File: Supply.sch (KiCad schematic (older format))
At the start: 7 parts, among them P5 CONN_01X02, Q5 AO3401, U3 EPL3015, U4 TPS61222

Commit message: Fix Boot0 pin and add prices per component
Signed-off-by: Philip Luyckx <philip.luyckx@gmail.com>
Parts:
- C8, C9: Price (none) -> 0.02
- Q5: Price (none) -> 0.06
- R11: Price (none) -> 0.01
- U3: Price (none) -> 1.15
- U4: Price (none) -> 1.00
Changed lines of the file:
@@
 F 2 "CustomSmd:SOT23" H 2900 2290 60  0001 C CNN
 F 3 "" H 2900 2290 60  0000 C CNN
+F 4 "0.06" H 3350 2150 60  0001 C CNN "Price"
 	1    3350 2150
 	0    1    -1   0
@@
 F 2 "Resistors_SMD:R_0603" V 2930 2450 30  0001 C CNN
 F 3 "" H 3000 2450 30  0000 C CNN
+F 4 "0.01" V 3000 2450 60  0001 C CNN "Price"
 	1    3000 2450
 	0    1    1    0
@@
 F 2 "Resistors_SMD:R_0805" H 3888 2150 30  0001 C CNN
 F 3 "" H 3850 2300 60  0000 C CNN
+F 4 "0.02" H 3850 2300 60  0001 C CNN "Price"
 	1    3850 2300
 	1    0    0    -1
@@
 F 2 "CustomInductors:EPL3015" H 4200 2050 60  0001 C CNN
 F 3 "" H 4200 2050 60  0000 C CNN
+F 4 "1.15" V 4200 2050 60  0001 C CNN "Price"
 	1    4200 2050
 	0    -1   -1   0
@@
 F 2 "Resistors_SMD:R_0805" H 5788 2050 30  0001 C CNN
 F 3 "" H 5750 2200 60  0000 C CNN
+F 4 "0.02" H 5750 2200 60  0001 C CNN "Price"
 	1    5750 2200
 	1    0    0    -1
@@
 F 2 "DC_DC_Converters:TPS6122x" H 4950 1900 60  0001 C CNN
 F 3 "" H 4950 1900 60  0000 C CNN
+F 4 "1.00" H 4950 1900 60  0001 C CNN "Price"
 	1    4950 1900
 	1    0    0    -1

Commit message: Update schematics for V3:
 * Change DHT22 to HTU21D
 * Change schematic for MCP6044
 * Correct unused opamp + power supply
 * Reassign some cpu pins (for HTU21D)
 * Add LDO power supply for 1.8V
 * Update STM32CubeMx project
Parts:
- added C17: 0.1uF, symbol C
- added C18: 0.47uF, symbol C
- added R15: 100k, symbol R
- added U4: TPS79718, symbol TPS79718
- renumbered C8 to C19, C9 to C20, P5 to P3, Q5 to Q2, R11 to R14, U3 to U5, U4 to U6
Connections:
- net +BATT: now also C17.1, U4.4 (IN)
- net GND: now also C17.2, C18.2, U4.2 (GND)
- new net: R15.1, U4.1 (PG)
- new net +1V8: C18.1, R15.2, U4.5 (OUT)
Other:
- note added: "1V8 Supply\n"
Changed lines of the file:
@@
 LIBS:CustomModules
 LIBS:CustomPower
-LIBS:CustomPowerConvertors
 LIBS:CustomTransistors
 LIBS:Custom_ShiftRegisters
@@
 LIBS:Relais
 LIBS:CustomDevices
+LIBS:CustomPowerConvertors
 LIBS:Sensor-cache
 EELAYER 25 0
@@
 $EndDescr
 $Comp
-L CONN_01X02 P5
+L CONN_01X02 P3
 U 1 1 56630FD4
 P 1800 2100
-F 0 "P5" H 1800 2250 50  0000 C CNN
+F 0 "P3" H 1800 2250 50  0000 C CNN
 F 1 "CONN_01X02" V 1900 2100 50  0000 C CNN
 F 2 "Socket_Strips:Socket_Strip_Straight_1x02" H 1800 2100 60  0001 C CNN
@@
 $EndComp
 $Comp
-L +BATT #PWR034
+L +BATT #PWR35
 U 1 1 56631049
 P 1600 2050
-F 0 "#PWR034" H 1600 1900 50  0001 C CNN
+F 0 "#PWR35" H 1600 1900 50  0001 C CNN
 F 1 "+BATT" H 1600 2190 50  0000 C CNN
 F 2 "" H 1600 2050 60  0000 C CNN
@@
 $EndComp
 $Comp
-L GND #PWR035
+L GND #PWR36
 U 1 1 5663105F
 P 1600 2150
-F 0 "#PWR035" H 1600 1900 50  0001 C CNN
+F 0 "#PWR36" H 1600 1900 50  0001 C CNN
 F 1 "GND" H 1600 2000 50  0000 C CNN
 F 2 "" H 1600 2150 60  0000 C CNN
@@
 	1400 2400 1400 1800
 $Comp
-L +BATT #PWR036
+L +BATT #PWR34
 U 1 1 56635CFE
 P 1500 1000
-F 0 "#PWR036" H 1500 850 50  0001 C CNN
+F 0 "#PWR34" H 1500 850 50  0001 C CNN
 F 1 "+BATT" H 1500 1140 50  0000 C CNN
 F 2 "" H 1500 1000 60  0000 C CNN
@@
 $EndComp
 $Comp
-L GND #PWR037
+L GND #PWR33
 U 1 1 56635D42
 P 1100 1050
-F 0 "#PWR037" H 1100 800 50  0001 C CNN
+F 0 "#PWR33" H 1100 800 50  0001 C CNN
 F 1 "GND" H 1100 900 50  0000 C CNN
 F 2 "" H 1100 1050 60  0000 C CNN
@@
 $EndComp
 $Comp
-L PWR_FLAG #FLG038
+L PWR_FLAG #FLG1
 U 1 1 56635D80
 P 1100 1050
-F 0 "#FLG038" H 1100 1145 50  0001 C CNN
+F 0 "#FLG1" H 1100 1145 50  0001 C CNN
 F 1 "PWR_FLAG" H 1100 1230 50  0000 C CNN
 F 2 "" H 1100 1050 60  0000 C CNN
@@
 $EndComp
 $Comp
-L PWR_FLAG #FLG039
+L PWR_FLAG #FLG2
 U 1 1 56635DC4
 P 1650 1000
-F 0 "#FLG039" H 1650 1095 50  0001 C CNN
+F 0 "#FLG2" H 1650 1095 50  0001 C CNN
 F 1 "PWR_FLAG" H 1650 1180 50  0000 C CNN
 F 2 "" H 1650 1000 60  0000 C CNN
@@
 $EndComp
 $Comp
-L +BATT #PWR040
+L +BATT #PWR38
 U 1 1 5664A279
 P 2850 2150
-F 0 "#PWR040" H 2850 2000 50  0001 C CNN
+F 0 "#PWR38" H 2850 2000 50  0001 C CNN
 F 1 "+BATT" H 2850 2290 50  0000 C CNN
 F 2 "" H 2850 2150 60  0000 C CNN
@@
 $EndComp
 $Comp
-L PMosfetGen Q5
+L PMosfetGen Q2
 U 1 1 5664A27A
 P 3350 2150
-F 0 "Q5" H 3575 2225 60  0000 C CNN
+F 0 "Q2" H 3575 2225 60  0000 C CNN
 F 1 "AO3401" H 3750 2125 60  0000 C CNN
 F 2 "CustomSmd:SOT23" H 2900 2290 60  0001 C CNN
@@
 $EndComp
 $Comp
-L R R11
+L R R14
 U 1 1 5664A27B
 P 3000 2450
-F 0 "R11" V 3080 2450 50  0000 C CNN
+F 0 "R14" V 3080 2450 50  0000 C CNN
 F 1 "47k" V 3000 2450 50  0000 C CNN
 F 2 "Resistors_SMD:R_0603" V 2930 2450 30  0001 C CNN
@@
 Enable5V
 $Comp
-L GND #PWR041
+L GND #PWR44
 U 1 1 5664A27D
 P 4500 2350
-F 0 "#PWR041" H 4500 2100 50  0001 C CNN
+F 0 "#PWR44" H 4500 2100 50  0001 C CNN
 F 1 "GND" H 4500 2200 50  0000 C CNN
 F 2 "" H 4500 2350 60  0000 C CNN
@@
 $EndComp
 $Comp
-L C C8
+L C C19
 U 1 1 5664A27E
 P 3850 2300
-F 0 "C8" H 3875 2400 50  0000 L CNN
+F 0 "C19" H 3875 2400 50  0000 L CNN
 F 1 "10uF" H 3875 2200 50  0000 L CNN
 F 2 "Resistors_SMD:R_0805" H 3888 2150 30  0001 C CNN
@@
 $EndComp
 $Comp
-L GND #PWR042
+L GND #PWR42
 U 1 1 5664A27F
 P 3850 2450
-F 0 "#PWR042" H 3850 2200 50  0001 C CNN
+F 0 "#PWR42" H 3850 2200 50  0001 C CNN
 F 1 "GND" H 3850 2300 50  0000 C CNN
 F 2 "" H 3850 2450 60  0000 C CNN
@@
 $EndComp
 $Comp
-L INDUCTOR U3
+L INDUCTOR U5
 U 1 1 5664A280
 P 4200 2050
-F 0 "U3" V 4150 2050 50  0000 C CNN
+F 0 "U5" V 4150 2050 50  0000 C CNN
 F 1 "EPL3015" V 4300 2050 50  0000 C CNN
 F 2 "CustomInductors:EPL3015" H 4200 2050 60  0001 C CNN
@@
 	5400 2050 6150 2050
 $Comp
-L C C9
+L C C20
 U 1 1 5664A281
 P 5750 2200
-F 0 "C9" H 5775 2300 50  0000 L CNN
+F 0 "C20" H 5775 2300 50  0000 L CNN
 F 1 "10uF" H 5775 2100 50  0000 L CNN
 F 2 "Resistors_SMD:R_0805" H 5788 2050 30  0001 C CNN
@@
 $EndComp
 $Comp
-L GND #PWR043
+L GND #PWR45
 U 1 1 5664A282
 P 5750 2350
-F 0 "#PWR043" H 5750 2100 50  0001 C CNN
+F 0 "#PWR45" H 5750 2100 50  0001 C CNN
 F 1 "GND" H 5750 2200 50  0000 C CNN
 F 2 "" H 5750 2350 60  0000 C CNN
@@
 Connection ~ 5750 2050
 $Comp
-L +5V #PWR044
+L +5V #PWR46
 U 1 1 5664A283
 P 6150 2050
-F 0 "#PWR044" H 6150 1900 50  0001 C CNN
+F 0 "#PWR46" H 6150 1900 50  0001 C CNN
 F 1 "+5V" H 6150 2190 50  0000 C CNN
 F 2 "" H 6150 2050 60  0000 C CNN
@@
 5V Supply
 $Comp
-L PWR_FLAG #FLG045
+L PWR_FLAG #FLG3
 U 1 1 5664A284
 P 3750 2000
-F 0 "#FLG045" H 3750 2095 50  0001 C CNN
+F 0 "#FLG3" H 3750 2095 50  0001 C CNN
 F 1 "PWR_FLAG" H 3750 2180 50  0000 C CNN
 F 2 "" H 3750 2000 60  0000 C CNN
@@
 	3750 2000 3750 2150
 $Comp
-L VCC #PWR046
+L VCC #PWR37
 U 1 1 5664A479
 P 1800 1000
-F 0 "#PWR046" H 1800 850 50  0001 C CNN
+F 0 "#PWR37" H 1800 850 50  0001 C CNN
 F 1 "VCC" H 1800 1150 50  0000 C CNN
 F 2 "" H 1800 1000 60  0000 C CNN
@@
 Connection ~ 1650 1000
 $Comp
-L TPS61222 U4
+L TPS61222 U6
 U 1 1 56687082
 P 4950 1900
-F 0 "U4" H 4950 1900 60  0000 C CNN
+F 0 "U6" H 4950 1900 60  0000 C CNN
 F 1 "TPS61222" H 4950 1350 60  0000 C CNN
 F 2 "DC_DC_Converters:TPS6122x" H 4950 1900 60  0001 C CNN
@@
 	1    0    0    -1
 $EndComp
+$Comp
+L TPS79718 U4
+U 1 1 5752E69A
+P 4050 4000
+F 0 "U4" H 4200 4050 60  0000 C CNN
+F 1 "TPS79718" H 4200 3650 60  0000 C CNN
+F 2 "" H 4200 4050 60  0000 C CNN
+F 3 "" H 4200 4050 60  0000 C CNN
+	1    4050 4000
+	-1   0    0    1
+$EndComp
+$Comp
+L +BATT #PWR40
+U 1 1 5752E781
+P 3500 3750
+F 0 "#PWR40" H 3500 3600 50  0001 C CNN
+F 1 "+BATT" H 3500 3890 50  0000 C CNN
+F 2 "" H 3500 3750 50  0000 C CNN
+F 3 "" H 3500 3750 50  0000 C CNN
+	1    3500 3750
+	1    0    0    -1
+$EndComp
+$Comp
+L C C18
+U 1 1 5752E7A5
+P 3200 4150
+F 0 "C18" H 3225 4250 50  0000 L CNN
+F 1 "0.47uF" H 3225 4050 50  0000 L CNN
+F 2 "" H 3238 4000 50  0000 C CNN
+F 3 "" H 3200 4150 50  0000 C CNN
+	1    3200 4150
+	1    0    0    -1
+$EndComp
+$Comp
+L GND #PWR39
+U 1 1 5752E7D6
+P 3200 4300
+F 0 "#PWR39" H 3200 4050 50  0001 C CNN
+F 1 "GND" H 3200 4150 50  0000 C CNN
+F 2 "" H 3200 4300 50  0000 C CNN
+F 3 "" H 3200 4300 50  0000 C CNN
+	1    3200 4300
+	1    0    0    -1
+$EndComp
+$Comp
+L GND #PWR43
+U 1 1 5752E81C
+P 4400 3850
+F 0 "#PWR43" H 4400 3600 50  0001 C CNN
+F 1 "GND" H 4400 3700 50  0000 C CNN
+F 2 "" H 4400 3850 50  0000 C CNN
+F 3 "" H 4400 3850 50  0000 C CNN
+	1    4400 3850
+	-1   0    0    1
+$EndComp
+Wire Wire Line
+	4250 3850 4400 3850
+$Comp
+L R R15
+U 1 1 5752E866
+P 3900 4250
+F 0 "R15" V 3980 4250 50  0000 C CNN
+F 1 "100k" V 3900 4250 50  0000 C CNN
+F 2 "" V 3830 4250 50  0000 C CNN
+F 3 "" H 3900 4250 50  0000 C CNN
+	1    3900 4250
+	0    1    1    0
+$EndComp
+Wire Wire Line
+	3200 3950 3500 3950
+Wire Wire Line
+	3500 3950 3500 4250
+Wire Wire Line
+	3500 4250 3750 4250
+Wire Wire Line
+	4050 4250 4250 4250
+Wire Wire Line
+	4250 4250 4250 3950
+Wire Wire Line
+	3200 3950 3200 4000
+$Comp
+L C C17
+U 1 1 5752EA4A
+P 2850 4150
+F 0 "C17" H 2875 4250 50  0000 L CNN
+F 1 "0.1uF" H 2875 4050 50  0000 L CNN
+F 2 "" H 2888 4000 50  0000 C CNN
+F 3 "" H 2850 4150 50  0000 C CNN
+	1    2850 4150
+	1    0    0    -1
+$EndComp
+Wire Wire Line
+	3500 3750 2850 3750
+Wire Wire Line
+	2850 3750 2850 4000
+Wire Wire Line
+	2850 4300 3200 4300
+Wire Notes Line
+	2600 3500 5000 3500
+Wire Notes Line
+	5000 3500 5000 4600
+Wire Notes Line
+	5000 4600 2600 4600
+Wire Notes Line
+	2600 4600 2600 3500
+Text Notes 2600 3500 0    60   ~ 0
+1V8 Supply\n
+$Comp
+L +1V8 #PWR41
+U 1 1 5753ACA5
+P 3500 3950
+F 0 "#PWR41" H 3500 3800 50  0001 C CNN
+F 1 "+1V8" H 3500 4090 50  0000 C CNN
+F 2 "" H 3500 3950 50  0000 C CNN
+F 3 "" H 3500 3950 50  0000 C CNN
+	1    3500 3950
+	1    0    0    -1
+$EndComp

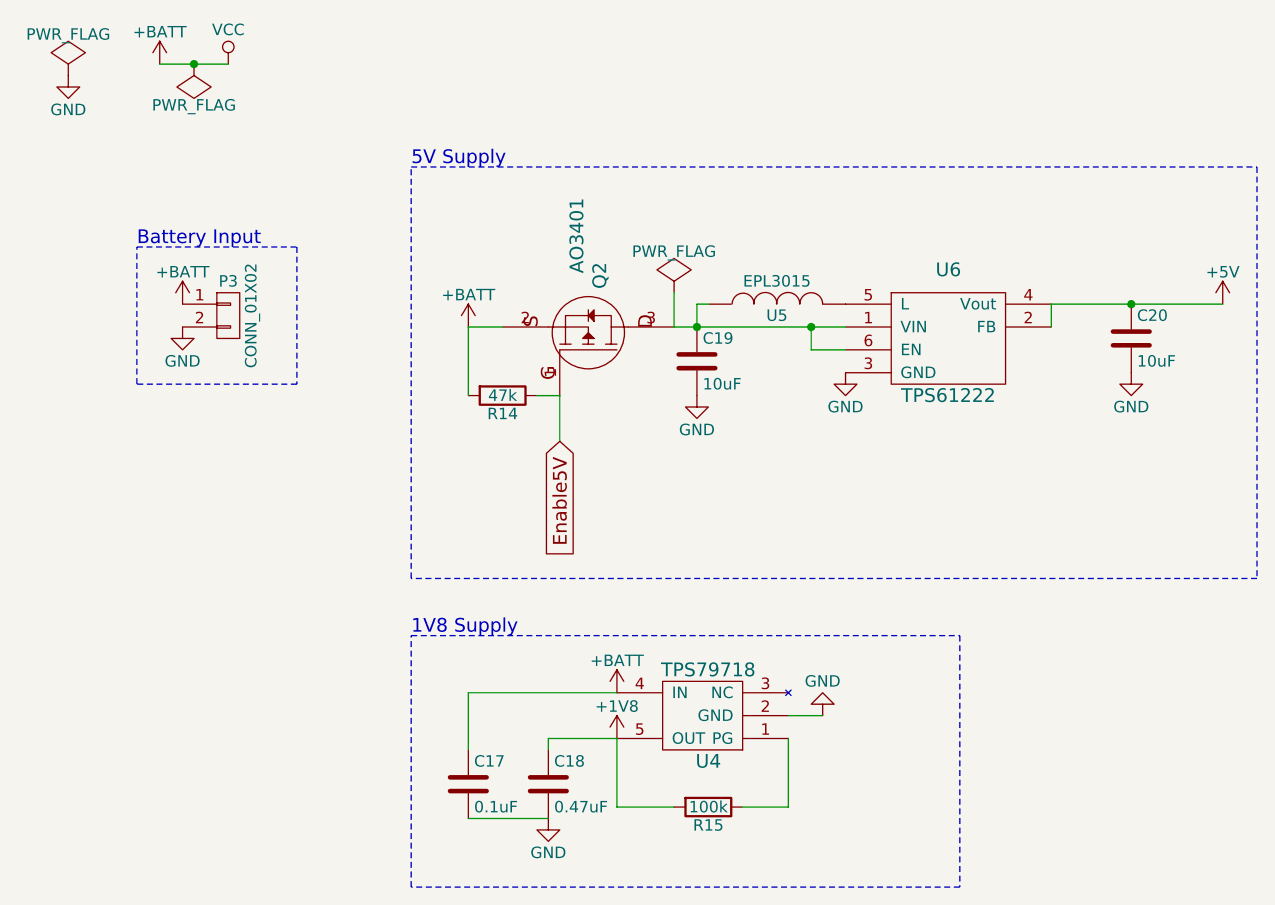
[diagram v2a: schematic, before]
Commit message: Updates for V3:
 * Remove unnecessary power supply enable MOSFETs
 * Optimize pin configuration

Signed-off-by: pluyckx <philip.luyckx@gmail.com>
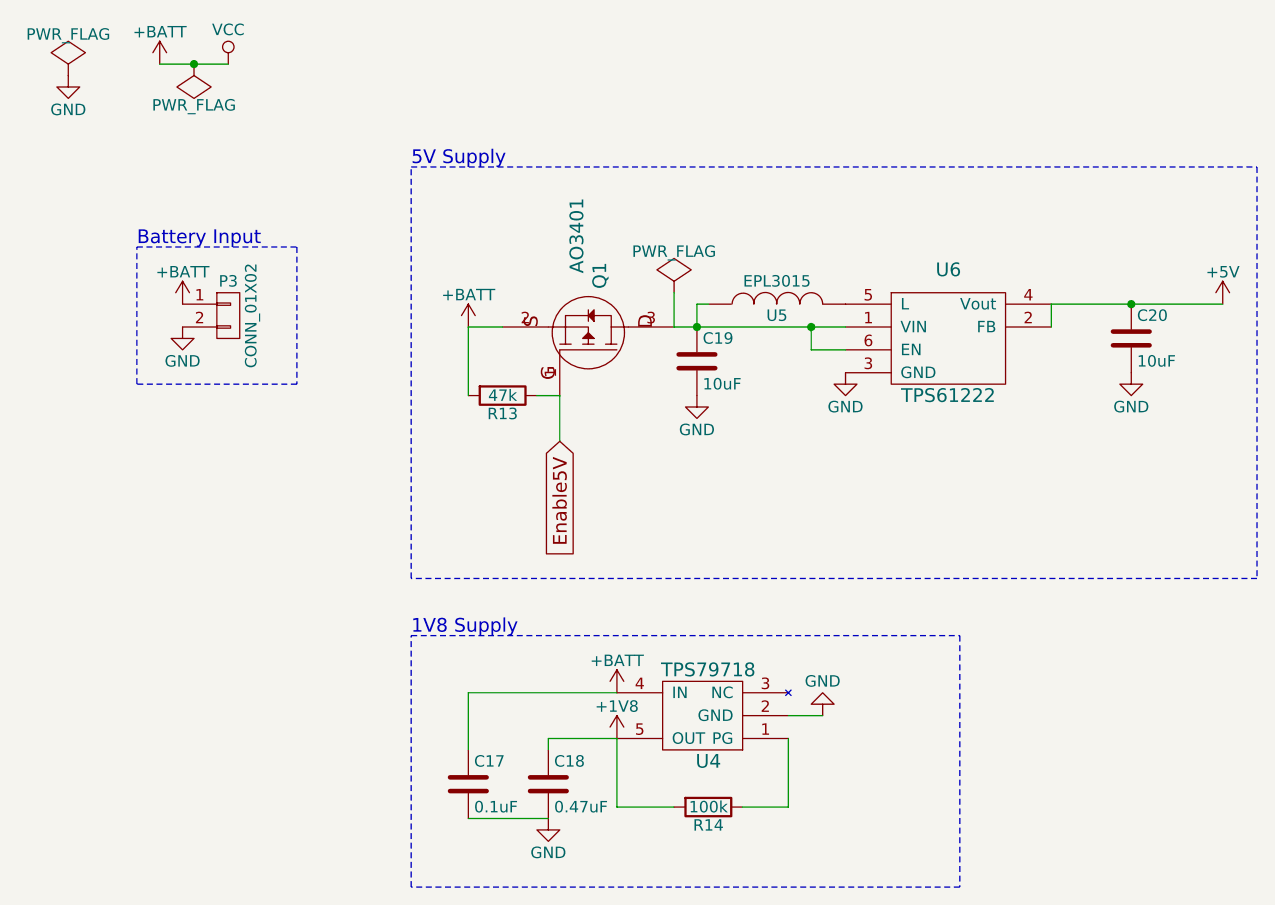
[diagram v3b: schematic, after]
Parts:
- renumbered Q2 to Q1, R14 to R13, R15 to R14
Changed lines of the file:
@@
 $EndComp
 $Comp
-L +BATT #PWR35
+L +BATT #PWR031
 U 1 1 56631049
 P 1600 2050
-F 0 "#PWR35" H 1600 1900 50  0001 C CNN
+F 0 "#PWR031" H 1600 1900 50  0001 C CNN
 F 1 "+BATT" H 1600 2190 50  0000 C CNN
 F 2 "" H 1600 2050 60  0000 C CNN
@@
 $EndComp
 $Comp
-L GND #PWR36
+L GND #PWR032
 U 1 1 5663105F
 P 1600 2150
-F 0 "#PWR36" H 1600 1900 50  0001 C CNN
+F 0 "#PWR032" H 1600 1900 50  0001 C CNN
 F 1 "GND" H 1600 2000 50  0000 C CNN
 F 2 "" H 1600 2150 60  0000 C CNN
@@
 	1400 2400 1400 1800
 $Comp
-L +BATT #PWR34
+L +BATT #PWR033
 U 1 1 56635CFE
 P 1500 1000
-F 0 "#PWR34" H 1500 850 50  0001 C CNN
+F 0 "#PWR033" H 1500 850 50  0001 C CNN
 F 1 "+BATT" H 1500 1140 50  0000 C CNN
 F 2 "" H 1500 1000 60  0000 C CNN
@@
 $EndComp
 $Comp
-L GND #PWR33
+L GND #PWR034
 U 1 1 56635D42
 P 1100 1050
-F 0 "#PWR33" H 1100 800 50  0001 C CNN
+F 0 "#PWR034" H 1100 800 50  0001 C CNN
 F 1 "GND" H 1100 900 50  0000 C CNN
 F 2 "" H 1100 1050 60  0000 C CNN
@@
 $EndComp
 $Comp
-L PWR_FLAG #FLG1
+L PWR_FLAG #FLG035
 U 1 1 56635D80
 P 1100 1050
-F 0 "#FLG1" H 1100 1145 50  0001 C CNN
+F 0 "#FLG035" H 1100 1145 50  0001 C CNN
 F 1 "PWR_FLAG" H 1100 1230 50  0000 C CNN
 F 2 "" H 1100 1050 60  0000 C CNN
@@
 $EndComp
 $Comp
-L PWR_FLAG #FLG2
+L PWR_FLAG #FLG036
 U 1 1 56635DC4
 P 1650 1000
-F 0 "#FLG2" H 1650 1095 50  0001 C CNN
+F 0 "#FLG036" H 1650 1095 50  0001 C CNN
 F 1 "PWR_FLAG" H 1650 1180 50  0000 C CNN
 F 2 "" H 1650 1000 60  0000 C CNN
@@
 $EndComp
 $Comp
-L +BATT #PWR38
+L +BATT #PWR037
 U 1 1 5664A279
 P 2850 2150
-F 0 "#PWR38" H 2850 2000 50  0001 C CNN
+F 0 "#PWR037" H 2850 2000 50  0001 C CNN
 F 1 "+BATT" H 2850 2290 50  0000 C CNN
 F 2 "" H 2850 2150 60  0000 C CNN
@@
 $EndComp
 $Comp
-L PMosfetGen Q2
+L PMosfetGen Q1
 U 1 1 5664A27A
 P 3350 2150
-F 0 "Q2" H 3575 2225 60  0000 C CNN
+F 0 "Q1" H 3575 2225 60  0000 C CNN
 F 1 "AO3401" H 3750 2125 60  0000 C CNN
 F 2 "CustomSmd:SOT23" H 2900 2290 60  0001 C CNN
@@
 $EndComp
 $Comp
-L R R14
+L R R13
 U 1 1 5664A27B
 P 3000 2450
-F 0 "R14" V 3080 2450 50  0000 C CNN
+F 0 "R13" V 3080 2450 50  0000 C CNN
 F 1 "47k" V 3000 2450 50  0000 C CNN
 F 2 "Resistors_SMD:R_0603" V 2930 2450 30  0001 C CNN
@@
 Enable5V
 $Comp
-L GND #PWR44
+L GND #PWR038
 U 1 1 5664A27D
 P 4500 2350
-F 0 "#PWR44" H 4500 2100 50  0001 C CNN
+F 0 "#PWR038" H 4500 2100 50  0001 C CNN
 F 1 "GND" H 4500 2200 50  0000 C CNN
 F 2 "" H 4500 2350 60  0000 C CNN
@@
 $EndComp
 $Comp
-L GND #PWR42
+L GND #PWR039
 U 1 1 5664A27F
 P 3850 2450
-F 0 "#PWR42" H 3850 2200 50  0001 C CNN
+F 0 "#PWR039" H 3850 2200 50  0001 C CNN
 F 1 "GND" H 3850 2300 50  0000 C CNN
 F 2 "" H 3850 2450 60  0000 C CNN
@@
 $EndComp
 $Comp
-L GND #PWR45
+L GND #PWR040
 U 1 1 5664A282
 P 5750 2350
-F 0 "#PWR45" H 5750 2100 50  0001 C CNN
+F 0 "#PWR040" H 5750 2100 50  0001 C CNN
 F 1 "GND" H 5750 2200 50  0000 C CNN
 F 2 "" H 5750 2350 60  0000 C CNN
@@
 Connection ~ 5750 2050
 $Comp
-L +5V #PWR46
+L +5V #PWR041
 U 1 1 5664A283
 P 6150 2050
-F 0 "#PWR46" H 6150 1900 50  0001 C CNN
+F 0 "#PWR041" H 6150 1900 50  0001 C CNN
 F 1 "+5V" H 6150 2190 50  0000 C CNN
 F 2 "" H 6150 2050 60  0000 C CNN
@@
 5V Supply
 $Comp
-L PWR_FLAG #FLG3
+L PWR_FLAG #FLG042
 U 1 1 5664A284
 P 3750 2000
-F 0 "#FLG3" H 3750 2095 50  0001 C CNN
+F 0 "#FLG042" H 3750 2095 50  0001 C CNN
 F 1 "PWR_FLAG" H 3750 2180 50  0000 C CNN
 F 2 "" H 3750 2000 60  0000 C CNN
@@
 	3750 2000 3750 2150
 $Comp
-L VCC #PWR37
+L VCC #PWR043
 U 1 1 5664A479
 P 1800 1000
-F 0 "#PWR37" H 1800 850 50  0001 C CNN
+F 0 "#PWR043" H 1800 850 50  0001 C CNN
 F 1 "VCC" H 1800 1150 50  0000 C CNN
 F 2 "" H 1800 1000 60  0000 C CNN
@@
 $EndComp
 $Comp
-L +BATT #PWR40
+L +BATT #PWR044
 U 1 1 5752E781
 P 3500 3750
-F 0 "#PWR40" H 3500 3600 50  0001 C CNN
+F 0 "#PWR044" H 3500 3600 50  0001 C CNN
 F 1 "+BATT" H 3500 3890 50  0000 C CNN
 F 2 "" H 3500 3750 50  0000 C CNN
@@
 $EndComp
 $Comp
-L GND #PWR39
+L GND #PWR045
 U 1 1 5752E7D6
 P 3200 4300
-F 0 "#PWR39" H 3200 4050 50  0001 C CNN
+F 0 "#PWR045" H 3200 4050 50  0001 C CNN
 F 1 "GND" H 3200 4150 50  0000 C CNN
 F 2 "" H 3200 4300 50  0000 C CNN
@@
 $EndComp
 $Comp
-L GND #PWR43
+L GND #PWR046
 U 1 1 5752E81C
 P 4400 3850
-F 0 "#PWR43" H 4400 3600 50  0001 C CNN
+F 0 "#PWR046" H 4400 3600 50  0001 C CNN
 F 1 "GND" H 4400 3700 50  0000 C CNN
 F 2 "" H 4400 3850 50  0000 C CNN
@@
 	4250 3850 4400 3850
 $Comp
-L R R15
+L R R14
 U 1 1 5752E866
 P 3900 4250
-F 0 "R15" V 3980 4250 50  0000 C CNN
+F 0 "R14" V 3980 4250 50  0000 C CNN
 F 1 "100k" V 3900 4250 50  0000 C CNN
 F 2 "" V 3830 4250 50  0000 C CNN
@@
 1V8 Supply\n
 $Comp
-L +1V8 #PWR41
+L +1V8 #PWR047
 U 1 1 5753ACA5
 P 3500 3950
-F 0 "#PWR41" H 3500 3800 50  0001 C CNN
+F 0 "#PWR047" H 3500 3800 50  0001 C CNN
 F 1 "+1V8" H 3500 4090 50  0000 C CNN
 F 2 "" H 3500 3950 50  0000 C CNN

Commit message: Finish schematic, assign all footprints for V3
Signed-off-by: pluyckx <philip.luyckx@gmail.com>
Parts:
- C17, C18: footprint (none) -> Resistors_SMD:R_0805
- R14: footprint (none) -> Resistors_SMD:R_0603
- U4: footprint (none) -> CustomSmd:SC70
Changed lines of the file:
@@
 encoding utf-8
 Sheet 6 6
-Title ""
-Date ""
-Rev ""
-Comp ""
+Title "Sensor"
+Date "2016-06-05"
+Rev "3"
+Comp "Philip Luyckx"
 Comment1 ""
 Comment2 ""
@@
 F 0 "U4" H 4200 4050 60  0000 C CNN
 F 1 "TPS79718" H 4200 3650 60  0000 C CNN
-F 2 "" H 4200 4050 60  0000 C CNN
+F 2 "CustomSmd:SC70" H 4200 4050 60  0001 C CNN
 F 3 "" H 4200 4050 60  0000 C CNN
 	1    4050 4000
@@
 F 0 "C18" H 3225 4250 50  0000 L CNN
 F 1 "0.47uF" H 3225 4050 50  0000 L CNN
-F 2 "" H 3238 4000 50  0000 C CNN
+F 2 "Resistors_SMD:R_0805" H 3238 4000 50  0001 C CNN
 F 3 "" H 3200 4150 50  0000 C CNN
 	1    3200 4150
@@
 F 0 "R14" V 3980 4250 50  0000 C CNN
 F 1 "100k" V 3900 4250 50  0000 C CNN
-F 2 "" V 3830 4250 50  0000 C CNN
+F 2 "Resistors_SMD:R_0603" V 3830 4250 50  0001 C CNN
 F 3 "" H 3900 4250 50  0000 C CNN
 	1    3900 4250
@@
 F 0 "C17" H 2875 4250 50  0000 L CNN
 F 1 "0.1uF" H 2875 4050 50  0000 L CNN
-F 2 "" H 2888 4000 50  0000 C CNN
+F 2 "Resistors_SMD:R_0805" H 2888 4000 50  0001 C CNN
 F 3 "" H 2850 4150 50  0000 C CNN
 	1    2850 4150
